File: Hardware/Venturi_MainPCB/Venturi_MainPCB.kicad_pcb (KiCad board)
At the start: 2 copper layers, 166.1 x 91.4 mm, 72 parts, among them J1 Battery, J2 ESC_PWM, J3 ESC_P, J4 ESC_N, J5 M1, J6 M1, J7 Sensor-PCB, Q1 BSS138, Q2 DMP3013SFV, SW1 POWER_EN, U1 TSOP38238, U2 ESP32-P4-WIFI6, U3 MIC29152WU, U4 DRV8212P, U5 DRV8212P, U6 ICM-42670-P

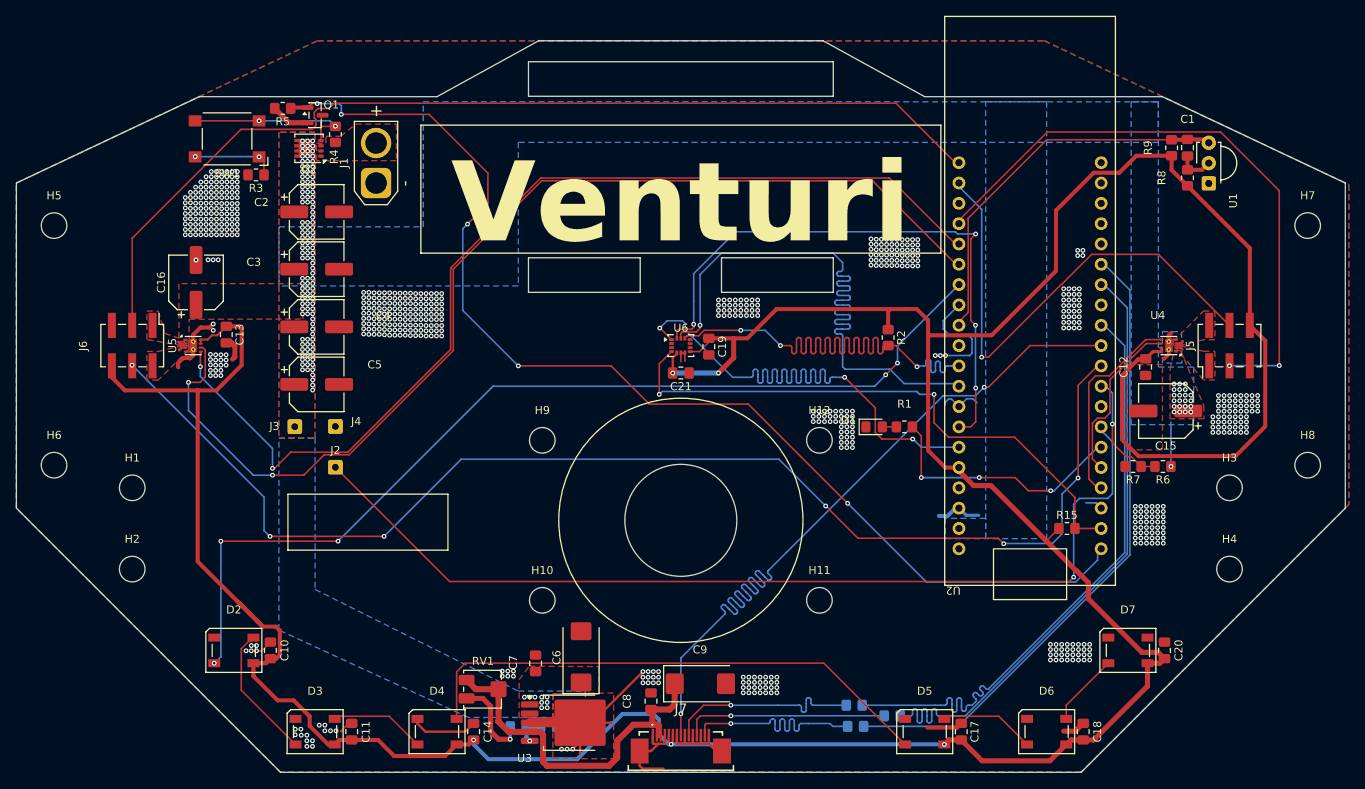
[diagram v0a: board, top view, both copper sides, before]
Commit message: Added Typst Documentation
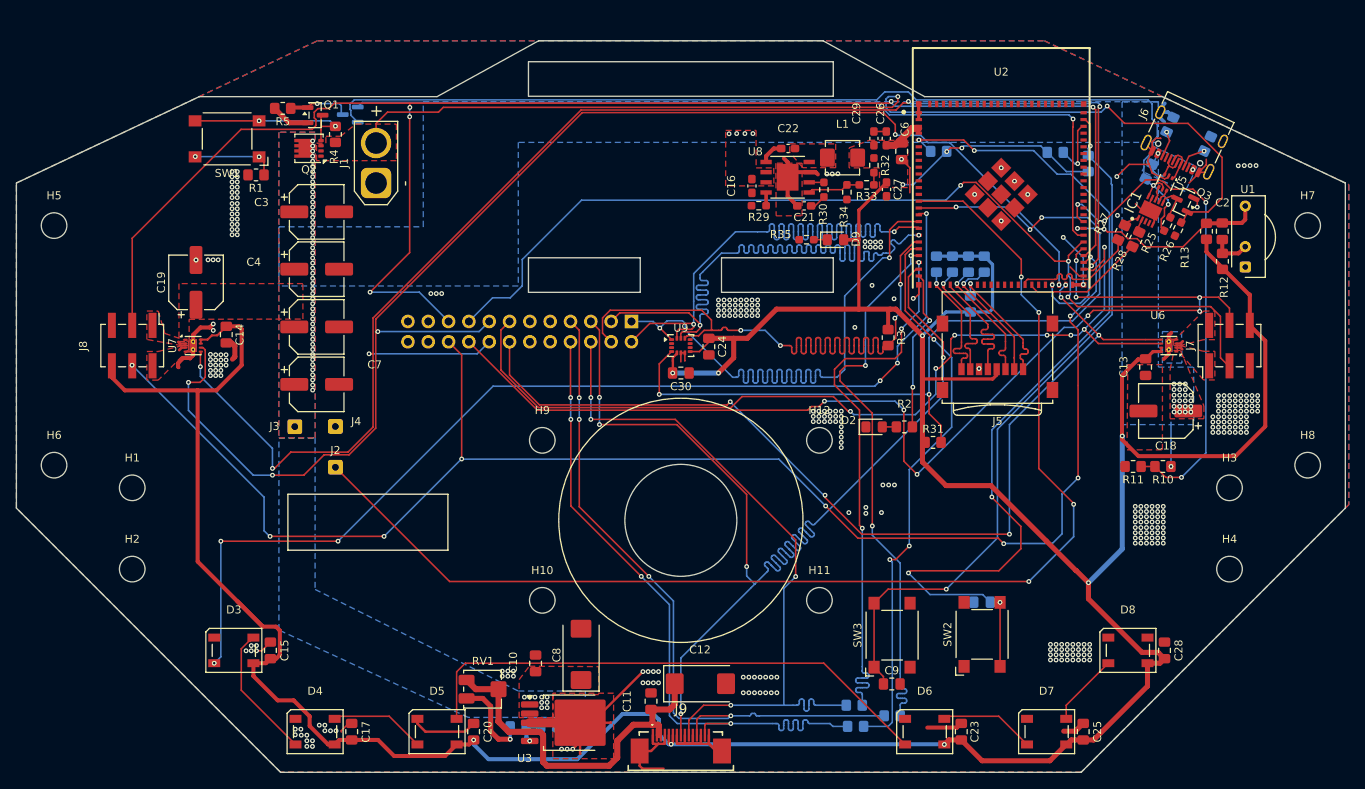
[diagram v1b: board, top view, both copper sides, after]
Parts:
- removed the R10 at (159.7, 136.9)
- removed the R11 at (164.3, 135.6)
- removed the R12 at (159.5, 134.2)
- added C1: 100n, Capacitor_SMD:C_0805_2012Metric_Pad1.18x1.45mm_HandSolder, B.Cu at (175.5, 121.4)
- added C16: 10u, Capacitor_SMD:C_0603_1608Metric_Pad1.08x0.95mm_HandSolder, F.Cu at (146.7, 69.3)
- added C21: 2.2n, Capacitor_SMD:C_0603_1608Metric_Pad1.08x0.95mm_HandSolder, F.Cu at (153.3, 71.8)
- added C22: 100n, Capacitor_SMD:C_0603_1608Metric_Pad1.08x0.95mm_HandSolder, F.Cu at (151.3, 64.6)
- added C26: 22u, Capacitor_SMD:C_0603_1608Metric_Pad1.08x0.95mm_HandSolder, F.Cu at (163.5, 63.4)
- added C27: 22u, Capacitor_SMD:C_0603_1608Metric_Pad1.08x0.95mm_HandSolder, F.Cu at (163.6, 69.8)
- added C29: 22u, Capacitor_SMD:C_0603_1608Metric_Pad1.08x0.95mm_HandSolder, F.Cu at (162.0, 63.4)
- added C6: 100n, Capacitor_SMD:C_0805_2012Metric_Pad1.18x1.45mm_HandSolder, F.Cu at (165.4, 65.0)
- added C9: 100n, Capacitor_SMD:C_0805_2012Metric_Pad1.18x1.45mm_HandSolder, F.Cu at (164.2, 131.6)
- added D1: BAT54C, Package_TO_SOT_SMD:SOT-23, B.Cu at (96.5, 60.4)
- added D9: LED, LED_SMD:LED_0805_2012Metric_Pad1.15x1.40mm_HandSolder, F.Cu at (157.2, 76.1)
- added F1: Fuse, Fuse:Fuse_0805_2012Metric_Pad1.15x1.40mm_HandSolder, B.Cu at (196.4, 67.5)
- added IC1: TS3USB221DRCR, Package_SON:SON50P300X300X100-11N-D, F.Cu at (196.6, 72.4)
- added J5: Micro_SD_Card, Connector_Card:microSD_HC_Wuerth_693072010801, F.Cu at (177.4, 90.7)
- added J6: USB_C_Receptacle_USB2.0_14P, Connector_USB:USB_C_Receptacle_G-Switch_GT-USB-7010ASV, F.Cu at (201.2, 62.9)
- added L1: 3u3, Inductor_SMD:L_Vishay_IHLP-1616, F.Cu at (158.1, 65.8)
- added Q3: BSS138, Package_TO_SOT_SMD:SOT-23, F.Cu at (200.7, 71.3)
- added R14: 10k, Resistor_SMD:R_0805_2012Metric_Pad1.20x1.40mm_HandSolder, B.Cu at (184.6, 65.1)
- added R15: 10k, Resistor_SMD:R_0805_2012Metric_Pad1.20x1.40mm_HandSolder, B.Cu at (188.8, 66.5)
- added R16: 10k, Resistor_SMD:R_0805_2012Metric_Pad1.20x1.40mm_HandSolder, B.Cu at (174.0, 84.1)
- added R17: 10k, Resistor_SMD:R_0805_2012Metric_Pad1.20x1.40mm_HandSolder, B.Cu at (175.8, 79.1)
- added R18: 10k, Resistor_SMD:R_0805_2012Metric_Pad1.20x1.40mm_HandSolder, B.Cu at (173.8, 79.1)
- added R19: 10k, Resistor_SMD:R_0805_2012Metric_Pad1.20x1.40mm_HandSolder, B.Cu at (171.8, 79.1)
- added R20: 10k, Resistor_SMD:R_0805_2012Metric_Pad1.20x1.40mm_HandSolder, B.Cu at (169.8, 79.1)
- added R23: 5k1, Resistor_SMD:R_0805_2012Metric_Pad1.20x1.40mm_HandSolder, B.Cu at (199.0, 61.7)
- added R24: 5k1, Resistor_SMD:R_0805_2012Metric_Pad1.20x1.40mm_HandSolder, B.Cu at (203.7, 64.1)
- added R25: 10k, Resistor_SMD:R_0603_1608Metric_Pad0.98x0.95mm_HandSolder, F.Cu at (198.6, 74.1)
- added R26: 10k, Resistor_SMD:R_0603_1608Metric_Pad0.98x0.95mm_HandSolder, F.Cu at (200.0, 74.7)
- added R27: 22R, Resistor_SMD:R_0805_2012Metric_Pad1.20x1.40mm_HandSolder, F.Cu at (192.9, 75.2)
- added R28: 22R, Resistor_SMD:R_0805_2012Metric_Pad1.20x1.40mm_HandSolder, F.Cu at (194.7, 76.0)
- added R29: 47k, Resistor_SMD:R_0603_1608Metric_Pad0.98x0.95mm_HandSolder, F.Cu at (147.6, 71.8)
- added R30: 15k, Resistor_SMD:R_0603_1608Metric_Pad0.98x0.95mm_HandSolder, F.Cu at (155.7, 69.8)
- added R32: 68k, Resistor_SMD:R_0603_1608Metric_Pad0.98x0.95mm_HandSolder, F.Cu at (162.0, 66.7)
- added R33: 1k, Resistor_SMD:R_0603_1608Metric_Pad0.98x0.95mm_HandSolder, F.Cu at (161.1, 69.2)
- added R34: 22k, Resistor_SMD:R_0603_1608Metric_Pad0.98x0.95mm_HandSolder, F.Cu at (158.6, 70.1)
- added R35: 330R, Resistor_SMD:R_0603_1608Metric_Pad0.98x0.95mm_HandSolder, F.Cu at (153.5, 76.0)
- added R6: 22R, Resistor_SMD:R_0805_2012Metric_Pad1.20x1.40mm_HandSolder, B.Cu at (159.7, 136.9)
- added R7: 22R, Resistor_SMD:R_0805_2012Metric_Pad1.20x1.40mm_HandSolder, B.Cu at (164.3, 135.6)
- added R8: 22R, Resistor_SMD:R_0805_2012Metric_Pad1.20x1.40mm_HandSolder, B.Cu at (159.5, 134.2)
- added R9: 10k, Resistor_SMD:R_0805_2012Metric_Pad1.20x1.40mm_HandSolder, B.Cu at (170.1, 65.0)
- added SW2: ESP_EN, Button_Switch_SMD:SW_SPST_Omron_B3FS-100xP, F.Cu at (175.5, 125.4)
- added SW3: ESP_BOOT, Button_Switch_SMD:SW_SPST_Omron_B3FS-100xP, F.Cu at (164.2, 125.5)
- added U4: SLogic16U3, Custom:SLogic16U3, B.Cu at (131.7, 87.5)
- added U5: USBLC6-2P6, Package_TO_SOT_SMD:SOT-666, F.Cu at (198.4, 68.9)
- added U8: AP64500SP-13, Package_SO:SO-8EP_DIO, F.Cu at (151.2, 68.2)
- J8: renamed from J6; value M1 -> M2
- U1: footprint OptoDevice:Vishay_MINICAST-3Pin -> OptoDevice:Vishay_CAST-3Pin
- U2: value ESP32-P4-WIFI6 -> ESP32-S31-WROOM-3; footprint RF_Module:ESP32-P4-WIFI6 -> RF_Module:ESP32-S31-WROOM-3
- moved R31 19.9 mm to (169.4, 101.4)
- moved U2 19.2 mm to (177.9, 70.4), turned to 0 degrees
- moved U1 11.4 mm to (208.4, 79.5)
- moved R12 11.3 mm to (205.5, 78.8)
- moved R13 11.3 mm to (203.5, 75.0)
- moved C2 11.3 mm to (205.5, 75.0)
- moved C8 0.31 mm to (125.4, 127.9)
- renumbered C7 to C10, C8 to C11, C9 to C12, C12 to C13, C13 to C14, C10 to C15, C11 to C17, C15 to C18, C16 to C19, C1 to C2, C14 to C20, C17 to C23, C19 to C24, C18 to C25, C20 to C28, C2 to C3, C21 to C30, C3 to C4, C4 to C5, C5 to C7, C6 to C8, D1 to D2, D2 to D3, D3 to D4, D4 to D5, D5 to D6, D6 to D7, D7 to D8, J5 to J7, J7 to J9, R3 to R1, R6 to R10, R7 to R11, R8 to R12, R9 to R13, R1 to R2, R13 to R21, R14 to R22, R2 to R3, R15 to R31, U4 to U6, U5 to U7, U6 to U9
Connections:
- net Net-(J1-Pin_2) renamed USB_EN
- Q1 pad 1: POWER_EN -> Net-(Q1-G)
- R2 pad 1: Net-(U2-GPIO29) -> Net-(U2-IO19)
- R5 pad 1: POWER_EN -> Net-(Q1-G)
- U2 pad 10: MISO -> unconnected-(U2-IO4-Pad10)
- U2 pad 13: IMU_MISO -> unconnected-(U2-IO7-Pad13)
- U2 pad 14: IMU_MOSI -> Net-(J2-Pin_1)
- U2 pad 15: IMU_CLK -> IR_SENSOR
- U2 pad 16: IMU_CS -> SK6812
- U2 pad 17: IR_SENSOR -> IMU_MISO
- U2 pad 18: SK6812 -> IMU_MOSI
- U2 pad 19: Net-(J2-Pin_1) -> IMU_CLK
- U2 pad 2: unconnected-(U2-USB_VBUS-Pad2) -> GND
- U2 pad 20: Net-(U2-GPIO29) -> IMU_CS
- U2 pad 21: MA_OUT_1 -> Net-(U2-IO15)
- U2 pad 22: MA_OUT_2 -> Net-(U2-IO16)
- U2 pad 23: MB_OUT_1 -> Net-(U2-IO17)
- U2 pad 24: MB_OUT_2 -> MISO
- U2 pad 25: MA_ENC_A -> Net-(U2-IO19)
- U2 pad 26: MA_ENC_B -> GND
- U2 pad 27: MB_ENC_A -> SD_D1
- U2 pad 28: MB_ENC_B -> SD_D0
- U2 pad 29: VBAT -> SD_CLK
- U2 pad 3: +BATT -> +3V3
- U2 pad 30: IMU_INT -> SD_CMD
- U2 pad 31: POWER_EN -> SD_D3
- U2 pad 32: unconnected-(U2-USB_D--Pad32) -> SD_D2
- U2 pad 33: unconnected-(U2-USB_D+-Pad33) -> GND
- U2 pad 4: unconnected-(U2-3V3_EN-Pad4) -> +3V3
- U2 pad 5: unconnected-(U2-ESP_EN-Pad5) -> Net-(U2-EN)
- U2 pad 6: +3V3 -> unconnected-(U2-IO2-Pad6)
- U2 pad 7: Net-(U2-GPIO2) -> unconnected-(U2-IO3-Pad7)
- U2 pad 8: Net-(U2-GPIO3) -> unconnected-(U2-IO0-Pad8)
- U2 pad 9: Net-(U2-GPIO4) -> unconnected-(U2-IO1-Pad9)
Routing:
- net USB_EN: track 0.00 -> 129.1 mm, vias 0 -> 2
- net VBUS: track 0.00 -> 126.4 mm, vias 0 -> 2
- net Net-(U2-EN): track 0.00 -> 115.5 mm, vias 0 -> 5
- net MA_OUT_2: track 24.9 -> 121.5 mm, vias 0 -> 6
- net MA_OUT_1: track 21.1 -> 117.0 mm, vias 0 -> 7
- net Net-(U2-IO61): track 0.00 -> 89.4 mm, vias 0 -> 2
- net Net-(U2-GPIO2): track 79.8 -> 0.00 mm
- net Net-(U2-GPIO4): track 78.9 -> 0.00 mm
- net Net-(U2-GPIO3): track 78.9 -> 0.00 mm
- net MA_ENC_B: track 63.2 -> 141.8 mm, vias 1 -> 8
- net MB_ENC_A: track 125.1 -> 196.2 mm, vias 0 -> 5
- net Net-(U2-IO15): track 0.00 -> 70.4 mm, vias 0 -> 3
- net Net-(U2-IO17): track 0.00 -> 70.3 mm, vias 0 -> 3
- net Net-(U2-IO16): track 0.00 -> 69.9 mm, vias 0 -> 3
- net MB_OUT_2: track 128.1 -> 196.4 mm, vias 2 -> 7
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- added copper zone on F.Cu, net +3V3
- added copper zone on In1.Cu, net GND
- added copper zone on In2.Cu, net GND
- added copper zone on B.Cu, net Net-(F1-Pad1)
- added copper zone on F.Cu, net Net-(U8-SW)
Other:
- copper layers 2 -> 4
- board text removed: "Venturi"

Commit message: Updated PCB fonts and part name and value placing
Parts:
- F1: value Fuse -> 500mA
- X5: renamed from J6; value USB_C_Receptacle_USB2.0_14P -> USB-C
- renumbered U9 to B1, C24 to C1, C2 to C13, C19 to C14, C14 to C15, C15 to C16, C20 to C18, C23 to C19, C30 to C2, C25 to C20, C28 to C21, C16 to C23, C26 to C24, C27 to C25, C29 to C26, C21 to C27, C6 to C28, C1 to C29, C9 to C30, C7 to C6, C18 to C7, C13 to C8, C8 to C9, U6 to D1, IC1 to D2, U7 to D3, D3 to D4, D4 to D5, D5 to D6, D6 to D7, D7 to D8, D8 to D9, H8 to H10, H10 to H11, D2 to H13, H9 to H8, H11 to H9, U3 to N1, U8 to N2, U2 to N3, U4 to P1, R4 to R1, R23 to R10, R24 to R11, R26 to R12, R21 to R13, R22 to R14, R12 to R15, R13 to R16, R16 to R17, R17 to R18, R18 to R19, R10 to R2, R19 to R20, R20 to R21, R32 to R22, R29 to R23, R30 to R24, R33 to R25, R35 to R26, R34 to R27, R9 to R28, R14 to R29, R31 to R3, R15 to R30, R3 to R31, R6 to R32, R7 to R33, R8 to R34, R2 to R35, R1 to R4, R11 to R6, R27 to R7, R28 to R8, R25 to R9, Q2 to V1, Q1 to V2, U5 to V3, D1 to V4, Q3 to V5, U1 to V6, D9 to V7, J3 to X1, J1 to X2, J4 to X3, J7 to X4, J8 to X6, J9 to X7, J5 to X8, J2 to X9
